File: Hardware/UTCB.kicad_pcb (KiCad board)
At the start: 4 copper layers, 98.6 x 135.4 mm, 89 parts, among them IC1 TR05S3V3, J1 Conn_01x02, J10 Conn_01x06, SW1 SW_DIP_x06

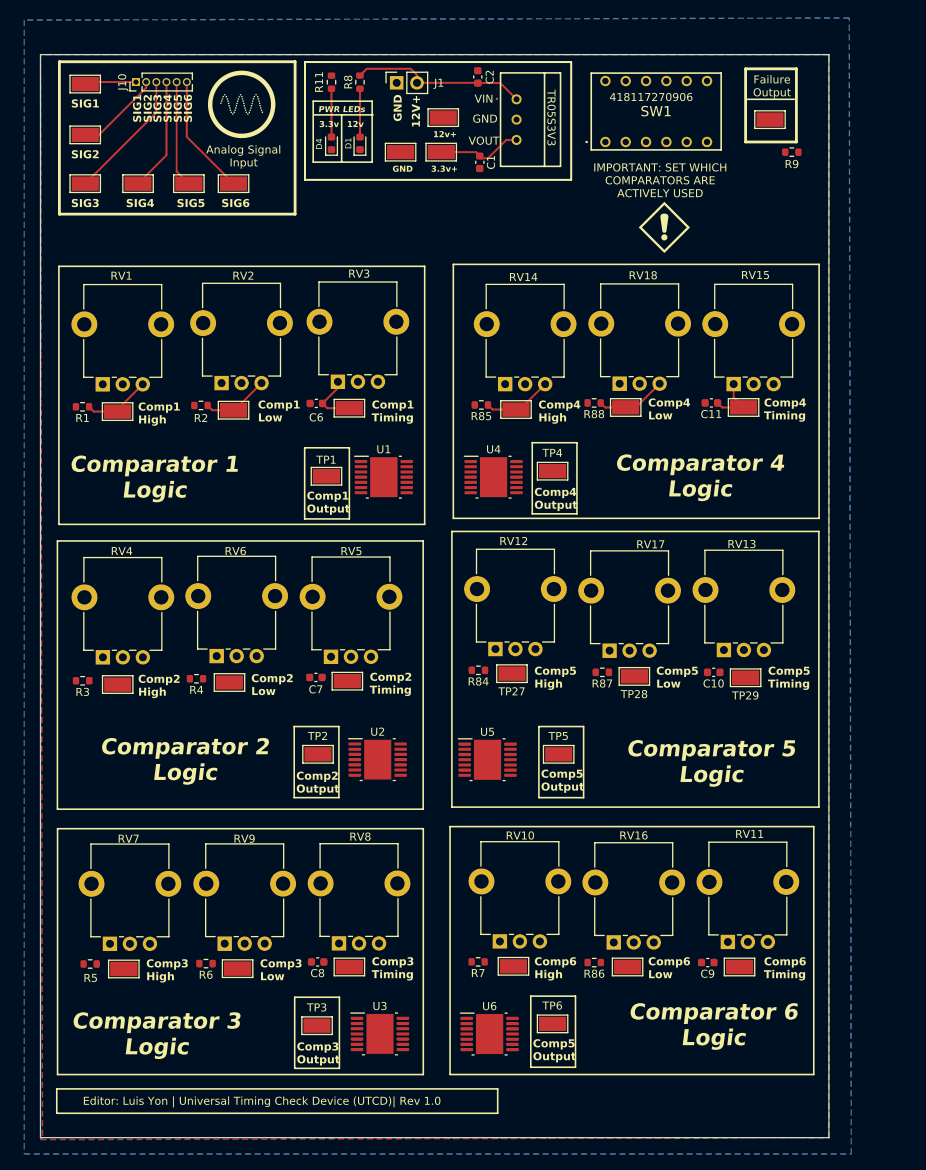
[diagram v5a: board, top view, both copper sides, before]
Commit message: Continued traces for layout
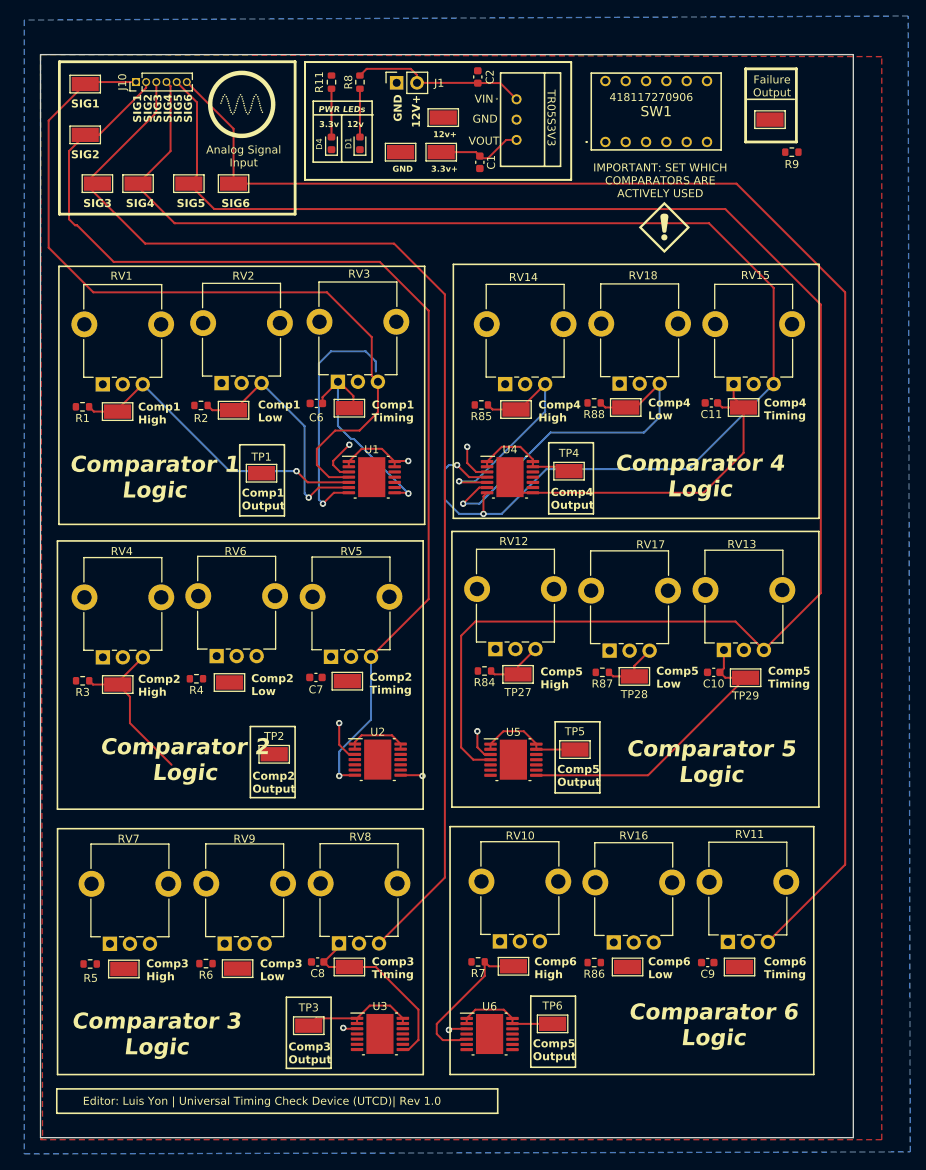
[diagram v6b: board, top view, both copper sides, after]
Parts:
- moved TP1 8.13 mm to (124.4, 73.9)
- moved TP2 5.48 mm to (126.0, 109.0)
- moved U5 3.23 mm to (155.9, 109.7)
- moved TP5 2.12 mm to (163.6, 108.5)
- moved U4 2.06 mm to (155.5, 74.4)
- moved TP4 2.06 mm to (162.8, 73.7)
- moved TP19 1.52 mm to (103.9, 37.7)
- moved U1 1.51 mm to (138.2, 74.4)
- moved TP3 1.04 mm to (130.3, 143.0)
- moved TP27 0.77 mm to (156.5, 99.1)
- moved R84 0.77 mm to (152.3, 98.6)
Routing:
- net Signal5: track 13.3 -> 203.9 mm
- net Signal6: track 15.1 -> 182.4 mm
- net Signal4: track 14.2 -> 173.0 mm, vias 0 -> 2
- net Signal3: track 16.4 -> 151.6 mm
- net Signal2: track 10.8 -> 136.6 mm, vias 0 -> 1
- net Signal1: track 6.46 -> 130.8 mm, vias 0 -> 1
- net /ComparatorLogic/Timing5Check: track 0.00 -> 37.7 mm
- net /ComparatorLogic/COMP4_LOW: track 8.83 -> 45.9 mm, vias 0 -> 1
- net /ComparatorLogic/Timing4Check: track 6.92 -> 43.1 mm
- net /ComparatorLogic/COMP1_HIGH: track 8.52 -> 39.4 mm, vias 0 -> 1
- net +3.3V: track 10.7 -> 34.5 mm, vias 0 -> 6
- net /ComparatorLogic/Timing3Check: track 0.00 -> 23.6 mm
- net /ComparatorLogic/COMP1_LOW: track 8.39 -> 30.7 mm, vias 0 -> 1
- net /ComparatorLogic/COMP4_HIGH: track 8.70 -> 30.0 mm, vias 0 -> 1
- net /ComparatorLogic/COMP2_HIGH: track 0.00 -> 21.3 mm
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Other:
- board size 98.6 x 135.4 mm -> 101.6 x 135.4 mm
